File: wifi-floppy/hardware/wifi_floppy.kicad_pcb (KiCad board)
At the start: 2 copper layers, 96 x 62 mm, 13 parts, among them J1 FLOPPY34, J2 PWR-BERG, Q1 BSS138, Q2 BSS138, Q3 BSS138, Q4 BSS138, Q5 BSS138, Q6 BSS138, U1 Pico2W/PicoPlus2W, U2 74LVC541A

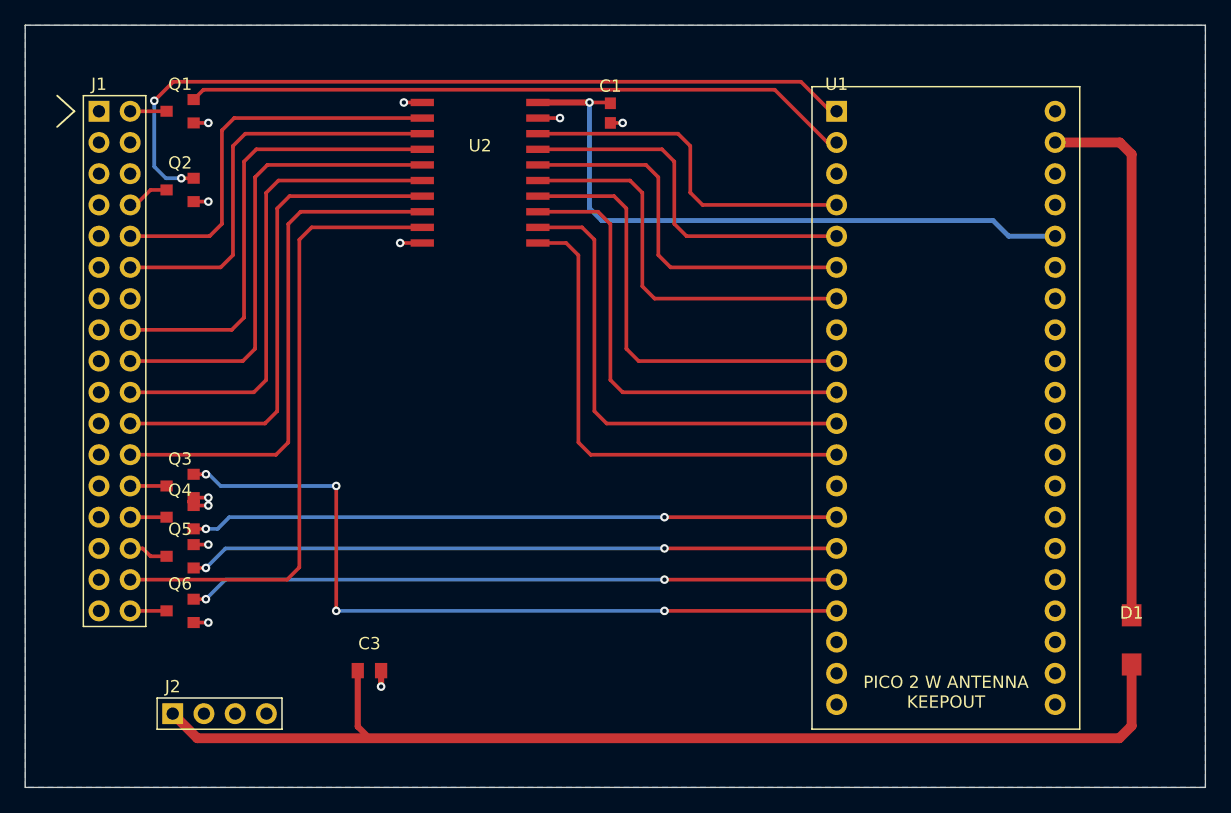
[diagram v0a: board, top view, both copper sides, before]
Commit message: Fix the reversed wifi-floppy PCB, and regenerate what it produces
The operator's fix, made in another session: the board was mirrored, so
a new revision had to be ordered. Hardware bring-up therefore slips to
the week of 2026-09-08 rather than this week.

Alongside the corrected wifi_floppy.kicad_pcb: both generator scripts,
the re-exported schematic and render, a regenerated bom.csv replacing
wifi_floppy_bom.csv/.ods, reference footprints, and a new
verify_board.py.

ONLY wifi-floppy/hardware/ is committed here. The firmware tree in the
working copy currently has 46 deletions -- transport_tls, token_store,
roots.h, the whole captive portal (portal_net, portal_http,
config_store, dhcp_server, dns_server) and the entire test directory
including run.sh -- with http_fetch.c restored, which plan 4a deleted as
the plaintext, path-addressed, credential-less fetcher. CMakeLists no
longer references any of the removed modules. Committing that would
erase plans 4a and 4b and reinstate the insecure fetcher, so it is left
untouched for the operator to resolve.

*.bak is gitignored rather than committed.

Co-Authored-By: Claude Opus 5 (1M context) <noreply@anthropic.com>
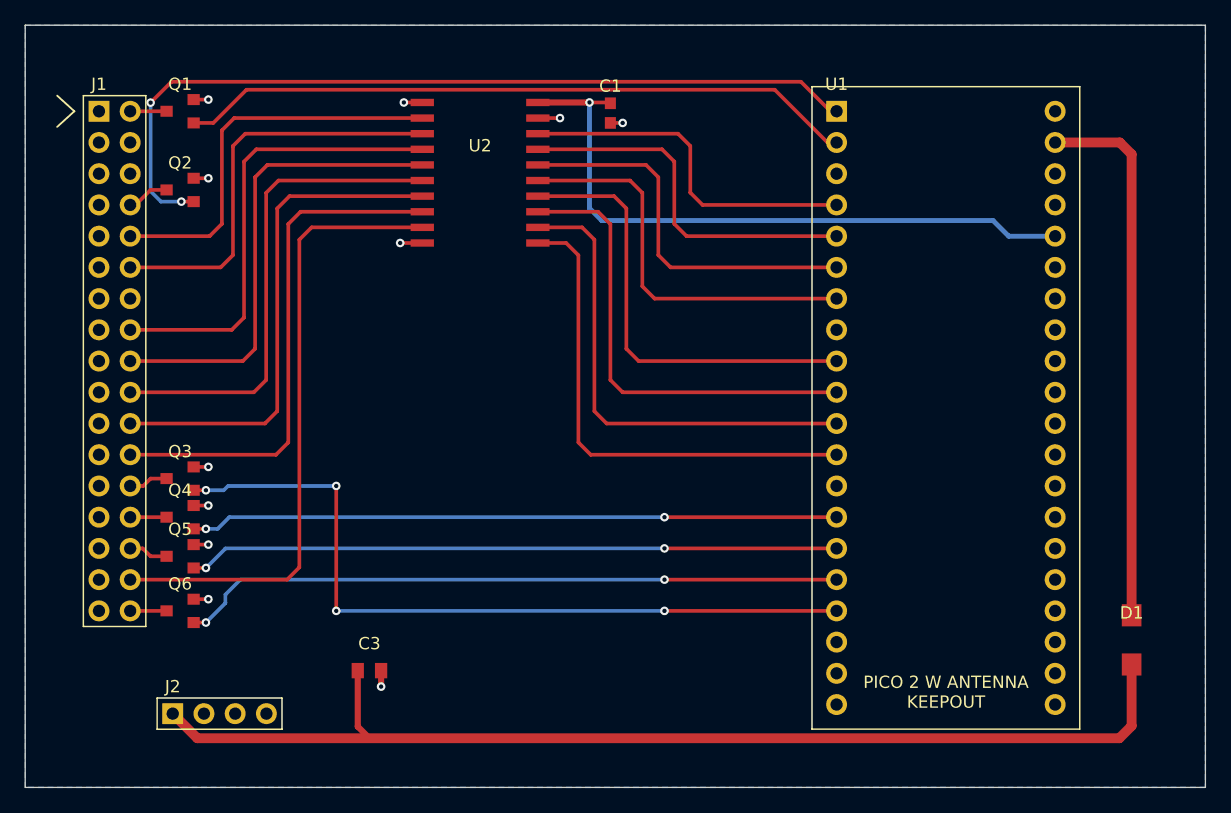
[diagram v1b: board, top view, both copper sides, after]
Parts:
- moved Q3 0.60 mm to (112.6, 136.9)
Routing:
- net INDEX: track 66.1 -> 68.6 mm
- net RDY: track 53.0 -> 54.1 mm
- net CHNG: track 54.4 -> 55.2 mm
